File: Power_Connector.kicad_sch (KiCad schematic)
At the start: 3 parts, among them J4 AMASS XT60 Male, J5 AMASS XT60 Female

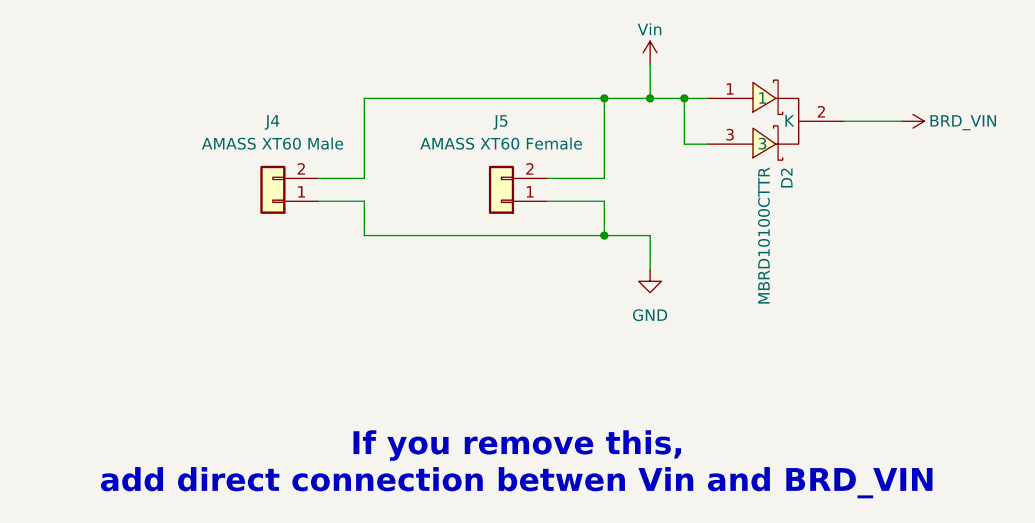
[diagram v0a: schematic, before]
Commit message: added rounded corners
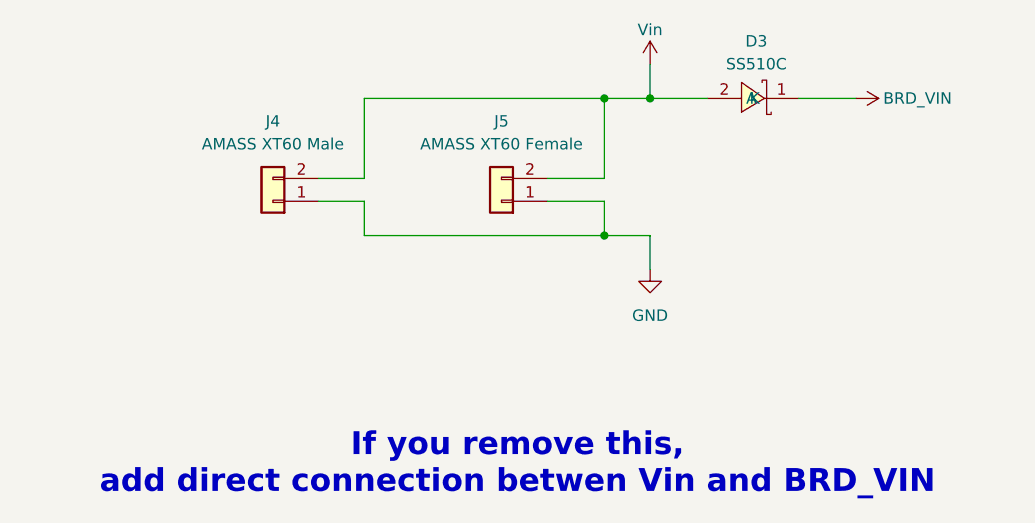
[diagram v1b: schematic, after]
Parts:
- removed D2: MBRD10100CTTR, SMC_MBRD10100CTTR:TO-252-3_L6.5-W5.8-P4.58-TL, symbol SMC_MBRD10100CTTR:MBRD10100CTTR
- added D3: SS510C, SS510C:SMC_L7.1-W6.2-LS8.1-RD, symbol SS510C:SS510C
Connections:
- net BRD_VIN: now also D3.1 (K)
- net Vin: now also D3.2 (A)
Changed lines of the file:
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@@
-	)
-	(junction
-		(at 161.29 86.36)
-		(diameter 0)
-		(color 0 0 0 0)
 	)
 	(junction
@@
 	(wire
 		(pts
-			(xy 161.29 86.36) (xy 163.83 86.36)
+			(xy 157.48 86.36) (xy 163.83 86.36)
 		)
 		(stroke
@@
 	(wire
 		(pts
-			(xy 157.48 86.36) (xy 161.29 86.36)
-		)
-		(stroke
-			(width 0)
-			(type default)
-		)
-	)
-	(wire
-		(pts
-			(xy 161.29 91.44) (xy 161.29 86.36)
-		)
-		(stroke
-			(width 0)
-			(type default)
-		)
-	)
-	(wire
-		(pts
-			(xy 163.83 91.44) (xy 161.29 91.44)
-		)
-		(stroke
-			(width 0)
-			(type default)
-		)
-	)
-	(wire
-		(pts
 			(xy 125.73 101.6) (xy 125.73 97.79)
 		)
@@
 	(wire
 		(pts
-			(xy 179.07 88.9) (xy 185.42 88.9)
+			(xy 173.99 86.36) (xy 180.34 86.36)
 		)
 		(stroke
@@
 	(symbol
 		(lib_id "power:VCC")
-		(at 185.42 88.9 270)
+		(at 180.34 86.36 270)
 		(unit 1)
 		(exclude_from_sim no)
@@
 		(dnp no)
 		(property "Reference" "#PWR041"
-			(at 181.61 88.9 0)
+			(at 176.53 86.36 0)
 			(effects
 				(font
@@
 		)
 		(property "Value" "BRD_VIN"
-			(at 192.278 88.9 90)
+			(at 187.198 86.36 90)
 			(effects
 				(font
@@
 		)
 		(property "Footprint" ""
-			(at 185.42 88.9 0)
+			(at 180.34 86.36 0)
 			(effects
 				(font
@@
 		)
 		(property "Datasheet" ""
-			(at 185.42 88.9 0)
+			(at 180.34 86.36 0)
 			(effects
 				(font
@@
 		)
 		(property "Description" "Power symbol creates a global label with name \"VCC\""
-			(at 185.42 88.9 0)
+			(at 180.34 86.36 0)
 			(effects
 				(font
@@
 	)
 	(symbol
-		(lib_id "SMC_MBRD10100CTTR:MBRD10100CTTR")
-		(at 171.45 88.9 0)
+		(lib_id "SS510C:SS510C")
+		(at 168.91 86.36 180)
 		(unit 1)
 		(exclude_from_sim no)
@@
 		(dnp no)
 		(fields_autoplaced yes)
-		(property "Reference" "D2"
-			(at 172.7201 93.98 90)
-			(effects
-				(font
-					(size 1.27 1.27)
-				)
-				(justify right)
-			)
-		)
-		(property "Value" "MBRD10100CTTR"
-			(at 170.1801 93.98 90)
-			(effects
-				(font
-					(size 1.27 1.27)
-				)
-				(justify right)
-			)
-		)
-		(property "Footprint" "SMC_MBRD10100CTTR:TO-252-3_L6.5-W5.8-P4.58-TL"
-			(at 171.45 99.06 0)
-			(effects
-				(font
-					(size 1.27 1.27)
-				)
-				(hide yes)
-			)
-		)
-		(property "Datasheet" "https://lcsc.com/product-detail/Schottky-Barrier-Diodes-SBD_MCC_MBRD10100CTTR_MBRD10100CTTR_C135494.html"
-			(at 171.45 101.6 0)
+		(property "Reference" "D3"
+			(at 169.29 80.01 0)
+			(effects
+				(font
+					(size 1.27 1.27)
+				)
+			)
+		)
+		(property "Value" "SS510C"
+			(at 169.29 82.55 0)
+			(effects
+				(font
+					(size 1.27 1.27)
+				)
+			)
+		)
+		(property "Footprint" "SS510C:SMC_L7.1-W6.2-LS8.1-RD"
+			(at 168.91 78.74 0)
+			(effects
+				(font
+					(size 1.27 1.27)
+				)
+				(hide yes)
+			)
+		)
+		(property "Datasheet" "https://lcsc.com/product-detail/Schottky-Barrier-Diodes-SBD_SS510C_C123944.html"
+			(at 168.91 76.2 0)
 			(effects
 				(font
@@
 		)
 		(property "Description" ""
-			(at 171.45 88.9 0)
-			(effects
-				(font
-					(size 1.27 1.27)
-				)
-				(hide yes)
-			)
-		)
-		(property "LCSC Part" "C135494"
-			(at 171.45 104.14 0)
-			(effects
-				(font
-					(size 1.27 1.27)
-				)
-				(hide yes)
-			)
-		)
-		(property "Sim.Device" ""
-			(at 171.45 88.9 90)
-			(effects
-				(font
-					(size 1.27 1.27)
-				)
-				(hide yes)
-			)
+			(at 168.91 86.36 0)
+			(effects
+				(font
+					(size 1.27 1.27)
+				)
+				(hide yes)
+			)
+		)
+		(property "Manufacturer" "晶导微电子"
+			(at 168.91 73.66 0)
+			(effects
+				(font
+					(size 1.27 1.27)
+				)
+				(hide yes)
+			)
+		)
+		(property "MPN" "SS510C"
+			(at 168.91 71.12 0)
+			(effects
+				(font
+					(size 1.27 1.27)
+				)
+				(hide yes)
+			)
+		)
+		(property "LCSC Part" "C123944"
+			(at 168.91 68.58 0)
+			(effects
+				(font
+					(size 1.27 1.27)
+				)
+				(hide yes)
+			)
+		)
+		(pin "2"
 		)
 		(pin "1"
 		)
-		(pin "2"
-		)
-		(pin "3"
-		)
 		(instances
-			(project "MMS3_hat_stepper_controler"
+			(project ""
 				(path "/6596548a-44e0-46d8-8624-fd71cf4a3e17/f11c3b61-ae6a-4858-9d37-bbf426f44fb0"
-					(reference "D2")
+					(reference "D3")
 					(unit 1)
 				)
